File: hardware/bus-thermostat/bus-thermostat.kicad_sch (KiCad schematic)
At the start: 0 parts

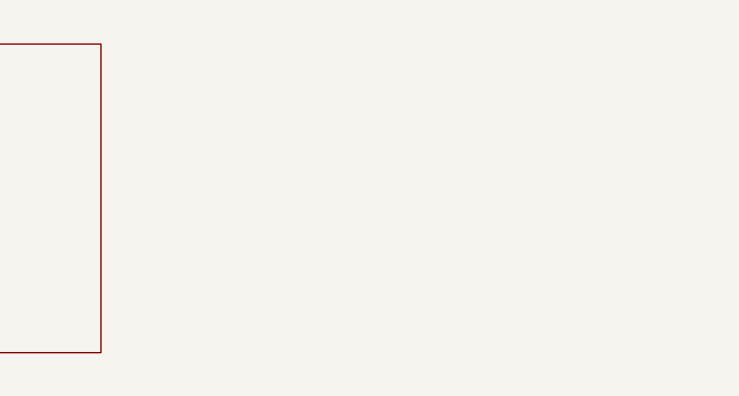
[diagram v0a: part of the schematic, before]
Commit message: Changing the SPWM around
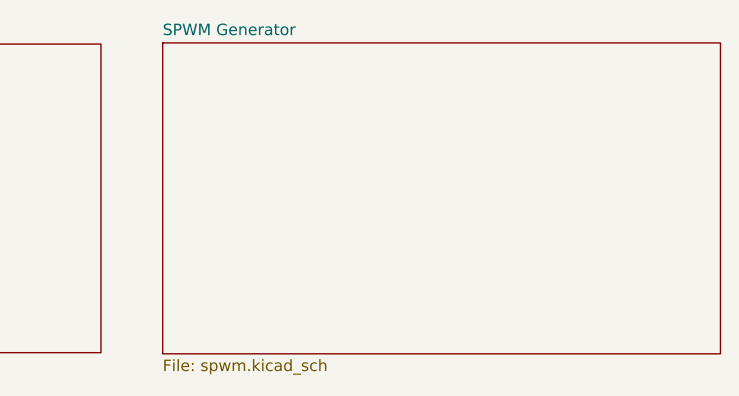
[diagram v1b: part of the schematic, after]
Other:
- added sheet SPWM Generator (spwm.kicad_sch)

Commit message: First rev of thermostat firmware
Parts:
- added J?: Screw_Terminal_01x02, symbol Connector:Screw_Terminal_01x02
- added J?: Screw_Terminal_01x04, symbol Connector:Screw_Terminal_01x04
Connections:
- new net +12V: J?.1 (Pin_1)
- new net C_wire: J?.4 (Pin_4)
- new net GND: J?.2 (Pin_2)
- new net G_wire: J?.1 (Pin_1)
- new net W_wire: J?.2 (Pin_2)
- new net Y_wire: J?.3 (Pin_3)
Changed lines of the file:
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@@
 (kicad_sch (version 20211123) (generator eeschema)
   (paper "A4")
+  (wire (pts (xy 49.022 101.473) (xy 65.786 101.473))
+    (stroke (width 0) (type default) (color 0 0 0 0))
+  )
+  (wire (pts (xy 65.786 113.157) (xy 63.5 113.157))
+    (stroke (width 0) (type default) (color 0 0 0 0))
+  )
+  (wire (pts (xy 49.022 98.933) (xy 65.786 98.933))
+    (stroke (width 0) (type default) (color 0 0 0 0))
+  )
+  (wire (pts (xy 63.5 115.697) (xy 65.786 115.697))
+    (stroke (width 0) (type default) (color 0 0 0 0))
+  )
+  (wire (pts (xy 49.022 96.393) (xy 65.786 96.393))
+    (stroke (width 0) (type default) (color 0 0 0 0))
+  )
+  (wire (pts (xy 63.5 110.871) (xy 63.5 113.157))
+    (stroke (width 0) (type default) (color 0 0 0 0))
+  )
+  (wire (pts (xy 63.5 118.11) (xy 63.5 115.697))
+    (stroke (width 0) (type default) (color 0 0 0 0))
+  )
+  (wire (pts (xy 49.149 104.013) (xy 65.786 104.013))
+    (stroke (width 0) (type default) (color 0 0 0 0))
+  )
+  (global_label "Y_wire" (shape input) (at 49.022 101.473 180) (fields_autoplaced)
+    (effects (font (size 1.27 1.27)) (justify right))
+    (property "Intersheet References" "${INTERSHEET_REFS}" (id 0) (at 40.7427 101.3936 0)
+      (effects (font (size 1.27 1.27)) (justify right) hide)
+    )
+  )
+  (global_label "W_wire" (shape input) (at 49.022 98.933 180) (fields_autoplaced)
+    (effects (font (size 1.27 1.27)) (justify right))
+    (property "Intersheet References" "${INTERSHEET_REFS}" (id 0) (at 40.3799 98.8536 0)
+      (effects (font (size 1.27 1.27)) (justify right) hide)
+    )
+  )
+  (global_label "C_wire" (shape input) (at 49.149 104.013 180) (fields_autoplaced)
+    (effects (font (size 1.27 1.27)) (justify right))
+    (property "Intersheet References" "${INTERSHEET_REFS}" (id 0) (at 40.6883 103.9336 0)
+      (effects (font (size 1.27 1.27)) (justify right) hide)
+    )
+  )
+  (global_label "G_wire" (shape input) (at 49.022 96.393 180) (fields_autoplaced)
+    (effects (font (size 1.27 1.27)) (justify right))
+    (property "Intersheet References" "${INTERSHEET_REFS}" (id 0) (at 40.5613 96.3136 0)
+      (effects (font (size 1.27 1.27)) (justify right) hide)
+    )
+  )
+  (symbol (lib_id "power:+12V") (at 63.5 110.871 0) (unit 1)
+    (in_bom yes) (on_board yes)
+    (property "Reference" "#PWR?" (id 0) (at 63.5 114.681 0)
+      (effects (font (size 1.27 1.27)) hide)
+    )
+    (property "Value" "+12V" (id 1) (at 62.992 107.061 0))
+    (property "Footprint" "" (id 2) (at 63.5 110.871 0)
+      (effects (font (size 1.27 1.27)) hide)
+    )
+    (property "Datasheet" "" (id 3) (at 63.5 110.871 0)
+      (effects (font (size 1.27 1.27)) hide)
+    )
+    (pin "1")
+  )
+  (symbol (lib_id "Connector:Screw_Terminal_01x02") (at 70.866 113.157 0) (unit 1)
+    (in_bom yes) (on_board yes) (fields_autoplaced)
+    (property "Reference" "J?" (id 0) (at 73.66 113.1569 0)
+      (effects (font (size 1.27 1.27)) (justify left))
+    )
+    (property "Value" "Screw_Terminal_01x02" (id 1) (at 73.66 115.6969 0)
+      (effects (font (size 1.27 1.27)) (justify left))
+    )
+    (property "Footprint" "" (id 2) (at 70.866 113.157 0)
+      (effects (font (size 1.27 1.27)) hide)
+    )
+    (property "Datasheet" "~" (id 3) (at 70.866 113.157 0)
+      (effects (font (size 1.27 1.27)) hide)
+    )
+    (pin "1")
+    (pin "2")
+  )
+  (symbol (lib_id "power:GND") (at 63.5 118.11 0) (unit 1)
+    (in_bom yes) (on_board yes)
+    (property "Reference" "#PWR?" (id 0) (at 63.5 124.46 0)
+      (effects (font (size 1.27 1.27)) hide)
+    )
+    (property "Value" "GND" (id 1) (at 63.5 122.174 0))
+    (property "Footprint" "" (id 2) (at 63.5 118.11 0)
+      (effects (font (size 1.27 1.27)) hide)
+    )
+    (property "Datasheet" "" (id 3) (at 63.5 118.11 0)
+      (effects (font (size 1.27 1.27)) hide)
+    )
+    (pin "1")
+  )
+  (symbol (lib_id "Connector:Screw_Terminal_01x04") (at 70.866 98.933 0) (unit 1)
+    (in_bom yes) (on_board yes) (fields_autoplaced)
+    (property "Reference" "J?" (id 0) (at 73.66 98.9329 0)
+      (effects (font (size 1.27 1.27)) (justify left))
+    )
+    (property "Value" "Screw_Terminal_01x04" (id 1) (at 73.66 101.4729 0)
+      (effects (font (size 1.27 1.27)) (justify left))
+    )
+    (property "Footprint" "" (id 2) (at 70.866 98.933 0)
+      (effects (font (size 1.27 1.27)) hide)
+    )
+    (property "Datasheet" "~" (id 3) (at 70.866 98.933 0)
+      (effects (font (size 1.27 1.27)) hide)
+    )
+    (pin "1")
+    (pin "2")
+    (pin "3")
+    (pin "4")
+  )
   (sheet (at 17.78 20.32) (size 55.88 34.29) (fields_autoplaced)
     (stroke (width 0.1524) (type solid) (color 0 0 0 0))
@@
       (reference "#PWR060") (unit 1) (value "GND") (footprint "")
     )
-    (path "/9a2fdddb-dad5-445e-a65c-2bfabfe3e5b9/95c2153b-4868-4c8f-873d-3268ea7ecfa7"
-      (reference "#PWR061") (unit 1) (value "+3V3") (footprint "")
-    )
-    (path "/9a2fdddb-dad5-445e-a65c-2bfabfe3e5b9/7ff05544-1504-476a-b892-5f01c5e034c4"
-      (reference "#PWR062") (unit 1) (value "GND") (footprint "")
-    )
     (path "/9a2fdddb-dad5-445e-a65c-2bfabfe3e5b9/a5f099e4-c633-414a-9719-1483d3540102"
       (reference "#PWR063") (unit 1) (value "GND") (footprint "")
@@
       (reference "#PWR0101") (unit 1) (value "-6V") (footprint "")
     )
+    (path "/e9a8718b-cce8-4a1a-9229-65779783a760/19e5e61e-4904-4fc2-a889-225a6f9529ad"
+      (reference "#PWR?") (unit 1) (value "GND") (footprint "")
+    )
+    (path "/2295b6ba-5c88-4e72-82fd-1de2cde8ad5c"
+      (reference "#PWR?") (unit 1) (value "+12V") (footprint "")
+    )
+    (path "/5225554a-3241-4eb4-9fd0-3f5061d0114a/2fb33cd7-f53e-4e9a-b1b4-f762c80e1ceb"
+      (reference "#PWR?") (unit 1) (value "GND") (footprint "")
+    )
+    (path "/5e83791a-22fa-4ad9-b200-df9a0fa51bd9"
+      (reference "#PWR?") (unit 1) (value "GND") (footprint "")
+    )
+    (path "/5225554a-3241-4eb4-9fd0-3f5061d0114a/8e31a8b0-9b04-4808-b7db-b4ea38283047"
+      (reference "#PWR?") (unit 1) (value "GND") (footprint "")
+    )
+    (path "/9a2fdddb-dad5-445e-a65c-2bfabfe3e5b9/9fe15f6f-8a99-4fe5-b2cb-39ca50568b71"
+      (reference "#PWR?") (unit 1) (value "+3V3") (footprint "")
+    )
+    (path "/9a2fdddb-dad5-445e-a65c-2bfabfe3e5b9/c767a628-9ce5-4e99-b0d6-9ffd51f2e266"
+      (reference "#PWR?") (unit 1) (value "GND") (footprint "")
+    )
+    (path "/5225554a-3241-4eb4-9fd0-3f5061d0114a/d0c84035-13b5-4e42-a768-c225322551a3"
+      (reference "#PWR?") (unit 1) (value "+3V3") (footprint "")
+    )
     (path "/5225554a-3241-4eb4-9fd0-3f5061d0114a/5416d296-3963-4899-9169-65cf2055b600"
       (reference "C1") (unit 1) (value "220pF") (footprint "")
@@
       (reference "C37") (unit 1) (value "100nF") (footprint "")
     )
+    (path "/b3446cb0-6e23-490d-8c96-4b8b72cbbdab/d8843b58-d803-4641-9b81-1964b29aca15"
+      (reference "C?") (unit 1) (value "470nF") (footprint "")
+    )
     (path "/5225554a-3241-4eb4-9fd0-3f5061d0114a/9921d59a-479e-4581-9892-34f37467aa18"
       (reference "D1") (unit 1) (value "LMB14S") (footprint "Diode_SMD:Diode_Bridge_Vishay_MBLS")
@@
       (reference "D12") (unit 1) (value "BAT54J") (footprint "Diode_SMD:D_SOD-323F")
     )
-    (path "/9a2fdddb-dad5-445e-a65c-2bfabfe3e5b9/a3d1acdc-5d8c-4ff6-8dae-71a976d7c1fc"
-      (reference "J1") (unit 1) (value "Conn_01x03_Female") (footprint "")
+    (path "/9a2fdddb-dad5-445e-a65c-2bfabfe3e5b9/739ce458-cbf7-4287-8a10-b8dd4eb792fe"
+      (reference "D?") (unit 1) (value "BAT42W-V") (footprint "Diode_SMD:D_SOD-123")
+    )
+    (path "/e9a8718b-cce8-4a1a-9229-65779783a760/ac1e7681-48cb-4190-8867-f5ff3d478e49"
+      (reference "D?") (unit 1) (value "18V Zener") (footprint "")
     )
     (path "/9a2fdddb-dad5-445e-a65c-2bfabfe3e5b9/fedf54aa-e23c-4192-8197-589a4b54af2f"
       (reference "J2") (unit 1) (value "RJ45_Shielded") (footprint "")
     )
+    (path "/58693072-0665-4444-9819-189d4fe97e8f"
+      (reference "J?") (unit 1) (value "Screw_Terminal_01x02") (footprint "")
+    )
+    (path "/71a196c3-2ba1-4e87-8601-8cd342758170"
+      (reference "J?") (unit 1) (value "Screw_Terminal_01x04") (footprint "")
+    )
+    (path "/9a2fdddb-dad5-445e-a65c-2bfabfe3e5b9/ec66682e-00f4-44dc-9e5e-2b2cdb8a8a1f"
+      (reference "J?") (unit 1) (value "FTDI Serial") (footprint "SparkFun-Connectors:6_PIN_SERIAL_TARGET_SIDE_W_SILK")
+    )
+    (path "/9a2fdddb-dad5-445e-a65c-2bfabfe3e5b9/d131077e-2109-4a2c-85dc-1939ce9a83fe"
+      (reference "JP?") (unit 1) (value "Solder Jumper") (footprint "Jumper:SolderJumper-2_P1.3mm_Open_TrianglePad1.0x1.5mm")
+    )
     (path "/5225554a-3241-4eb4-9fd0-3f5061d0114a/b9509bd5-25af-4378-b6b0-d098fb79c657"
       (reference "L1") (unit 1) (value "100mH") (footprint "")
@@
       (reference "R46") (unit 1) (value "10k") (footprint "")
     )
+    (path "/9a2fdddb-dad5-445e-a65c-2bfabfe3e5b9/10990986-19d1-4e7a-87b5-88d2b2cd50b8"
+      (reference "R?") (unit 1) (value "470R") (footprint "")
+    )
+    (path "/5225554a-3241-4eb4-9fd0-3f5061d0114a/7e4d14b9-ef9a-4b98-af8f-b239a9ae5175"
+      (reference "R?") (unit 1) (value "10k") (footprint "")
+    )
+    (path "/5225554a-3241-4eb4-9fd0-3f5061d0114a/c372fdac-807e-4682-a91c-559f1b825eaa"
+      (reference "R?") (unit 1) (value "10k") (footprint "")
+    )
     (path "/b3446cb0-6e23-490d-8c96-4b8b72cbbdab/eeac21de-3d26-4236-8cca-48baa88e445a"
       (reference "RV1") (unit 1) (value "50k") (footprint "")
@@
       (reference "U14") (unit 1) (value "TLV9301IDCK") (footprint "Package_TO_SOT_SMD:SOT-353_SC-70-5")
     )
-  )
+    (path "/5225554a-3241-4eb4-9fd0-3f5061d0114a/0ba209e5-47d3-4e1d-b5c2-2758757a26c8"
+      (reference "U?") (unit 1) (value "PCA9557D") (footprint "Package_SO:SOP-16_3.9x9.9mm_P1.27mm")
+    )
+  )

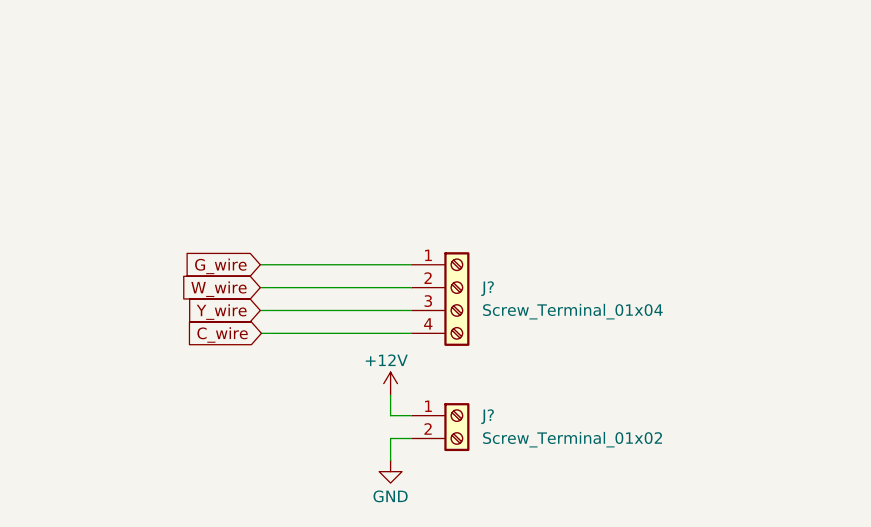
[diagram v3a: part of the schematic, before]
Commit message: OK, we will need the R wire!  Also put in option to use 12VDC
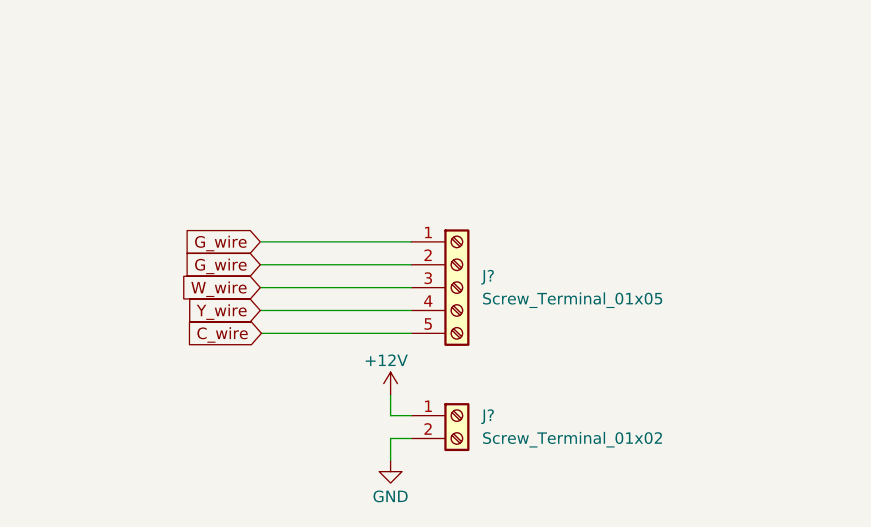
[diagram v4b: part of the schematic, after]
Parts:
- removed J?: Screw_Terminal_01x04, symbol Connector:Screw_Terminal_01x04
- added J?: Screw_Terminal_01x05, TerminalBlock_TE-Connectivity:TerminalBlock_TE_282834-5_1x05_P2.54mm_Horizontal, symbol Connector:Screw_Terminal_01x05
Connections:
- net C_wire: now also J?.5 (Pin_5)
- net G_wire: now also J?.2 (Pin_2)
- net W_wire: now also J?.3 (Pin_3)
- net Y_wire: now also J?.4 (Pin_4)
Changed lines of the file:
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@@
+    (stroke (width 0) (type default) (color 0 0 0 0))
+  )
+  (wire (pts (xy 49.149 93.853) (xy 65.786 93.853))
     (stroke (width 0) (type default) (color 0 0 0 0))
   )
@@
   (wire (pts (xy 49.149 104.013) (xy 65.786 104.013))
     (stroke (width 0) (type default) (color 0 0 0 0))
+  )
+  (global_label "G_wire" (shape input) (at 49.022 93.853 180) (fields_autoplaced)
+    (effects (font (size 1.27 1.27)) (justify right))
+    (property "Intersheet References" "${INTERSHEET_REFS}" (id 0) (at 40.5613 93.7736 0)
+      (effects (font (size 1.27 1.27)) (justify right) hide)
+    )
   )
   (global_label "Y_wire" (shape input) (at 49.022 101.473 180) (fields_autoplaced)
@@
     (pin "1")
   )
+  (symbol (lib_id "Connector:Screw_Terminal_01x05") (at 70.866 98.933 0) (unit 1)
+    (in_bom yes) (on_board yes) (fields_autoplaced)
+    (property "Reference" "J?" (id 0) (at 73.66 97.6629 0)
+      (effects (font (size 1.27 1.27)) (justify left))
+    )
+    (property "Value" "Screw_Terminal_01x05" (id 1) (at 73.66 100.2029 0)
+      (effects (font (size 1.27 1.27)) (justify left))
+    )
+    (property "Footprint" "TerminalBlock_TE-Connectivity:TerminalBlock_TE_282834-5_1x05_P2.54mm_Horizontal" (id 2) (at 70.866 98.933 0)
+      (effects (font (size 1.27 1.27)) hide)
+    )
+    (property "Datasheet" "~" (id 3) (at 70.866 98.933 0)
+      (effects (font (size 1.27 1.27)) hide)
+    )
+    (pin "1")
+    (pin "2")
+    (pin "3")
+    (pin "4")
+    (pin "5")
+  )
   (symbol (lib_id "Connector:Screw_Terminal_01x02") (at 70.866 113.157 0) (unit 1)
     (in_bom yes) (on_board yes) (fields_autoplaced)
@@
     )
     (pin "1")
-  )
-  (symbol (lib_id "Connector:Screw_Terminal_01x04") (at 70.866 98.933 0) (unit 1)
-    (in_bom yes) (on_board yes) (fields_autoplaced)
-    (property "Reference" "J?" (id 0) (at 73.66 98.9329 0)
-      (effects (font (size 1.27 1.27)) (justify left))
-    )
-    (property "Value" "Screw_Terminal_01x04" (id 1) (at 73.66 101.4729 0)
-      (effects (font (size 1.27 1.27)) (justify left))
-    )
-    (property "Footprint" "" (id 2) (at 70.866 98.933 0)
-      (effects (font (size 1.27 1.27)) hide)
-    )
-    (property "Datasheet" "~" (id 3) (at 70.866 98.933 0)
-      (effects (font (size 1.27 1.27)) hide)
-    )
-    (pin "1")
-    (pin "2")
-    (pin "3")
-    (pin "4")
   )
   (sheet (at 17.78 20.32) (size 55.88 34.29) (fields_autoplaced)
@@
       (reference "#PWR?") (unit 1) (value "GND") (footprint "")
     )
+    (path "/5225554a-3241-4eb4-9fd0-3f5061d0114a/62a3a113-d718-4984-ab2a-c3bee3378b07"
+      (reference "#PWR?") (unit 1) (value "GND") (footprint "")
+    )
     (path "/5225554a-3241-4eb4-9fd0-3f5061d0114a/8e31a8b0-9b04-4808-b7db-b4ea38283047"
       (reference "#PWR?") (unit 1) (value "GND") (footprint "")
@@
       (reference "#PWR?") (unit 1) (value "+3V3") (footprint "")
     )
+    (path "/5225554a-3241-4eb4-9fd0-3f5061d0114a/e2b27fb8-853c-4b7f-b30d-7f8909fd54ae"
+      (reference "#PWR?") (unit 1) (value "+12V") (footprint "")
+    )
     (path "/5225554a-3241-4eb4-9fd0-3f5061d0114a/5416d296-3963-4899-9169-65cf2055b600"
       (reference "C1") (unit 1) (value "220pF") (footprint "")
@@
       (reference "J2") (unit 1) (value "RJ45_Shielded") (footprint "")
     )
+    (path "/545e4862-bb1c-4821-8a9a-7c01d0d7fc54"
+      (reference "J?") (unit 1) (value "Screw_Terminal_01x05") (footprint "TerminalBlock_TE-Connectivity:TerminalBlock_TE_282834-5_1x05_P2.54mm_Horizontal")
+    )
     (path "/58693072-0665-4444-9819-189d4fe97e8f"
       (reference "J?") (unit 1) (value "Screw_Terminal_01x02") (footprint "")
     )
-    (path "/71a196c3-2ba1-4e87-8601-8cd342758170"
-      (reference "J?") (unit 1) (value "Screw_Terminal_01x04") (footprint "")
-    )
     (path "/9a2fdddb-dad5-445e-a65c-2bfabfe3e5b9/ec66682e-00f4-44dc-9e5e-2b2cdb8a8a1f"
       (reference "J?") (unit 1) (value "FTDI Serial") (footprint "SparkFun-Connectors:6_PIN_SERIAL_TARGET_SIDE_W_SILK")
     )
+    (path "/5225554a-3241-4eb4-9fd0-3f5061d0114a/6e598c97-8aff-43bd-b808-c90588d83f49"
+      (reference "JP?") (unit 1) (value "Solder Jumper") (footprint "Jumper:SolderJumper-3_P2.0mm_Open_TrianglePad1.0x1.5mm")
+    )
     (path "/9a2fdddb-dad5-445e-a65c-2bfabfe3e5b9/d131077e-2109-4a2c-85dc-1939ce9a83fe"
       (reference "JP?") (unit 1) (value "Solder Jumper") (footprint "Jumper:SolderJumper-2_P1.3mm_Open_TrianglePad1.0x1.5mm")
     )
+    (path "/5225554a-3241-4eb4-9fd0-3f5061d0114a/f602393b-284c-4f43-8b11-507c4fa137ca"
+      (reference "JP?") (unit 1) (value "Solder Jumper") (footprint "Jumper:SolderJumper-3_P2.0mm_Open_TrianglePad1.0x1.5mm")
+    )
     (path "/5225554a-3241-4eb4-9fd0-3f5061d0114a/b9509bd5-25af-4378-b6b0-d098fb79c657"
